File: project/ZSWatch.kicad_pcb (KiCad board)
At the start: 4 copper layers, 41 x 38 mm, 74 parts, among them IC1 nPM1300-QEXX, IC10 DRV2603RUNT, IC11 FAN5622SX, IC2 APDS-9306-065, IC3 BMI270, IC4 BMP581, IC5 BME688, IC6 LIS2MDLTR, IC7 ESDALC6V1W5, IC8 AT25SL128A, IC9 NTS0104GU12, M1 NORA-B106, Q1 BC817W, X1 BATTERY, X2 DOCK, X3 GC9A01A_CST816S, X4 M+, X5 M-

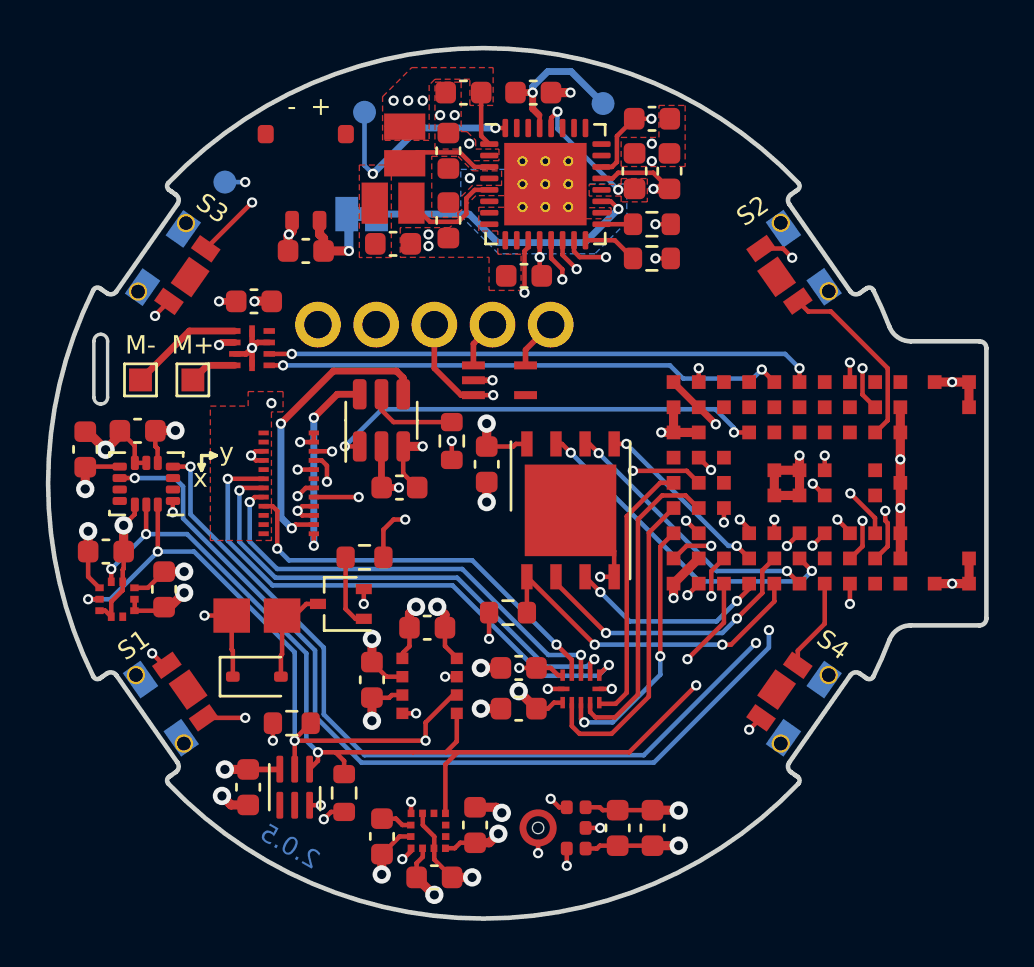
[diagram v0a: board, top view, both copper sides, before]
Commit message: - Add QR code library with link to the project - Change ISET resistor to 12k - Replace light sensor footprint with a version from our KiCad library - Rename the inner copper layers - Add KiBot file for production file generation - Import nPM1300 from test project - Remove pull down resistor from vibration driver IC enable - Split schematics into hierarical schematics - Add PCB variant for reduced sensor board - Add I2S microphone - Update all symbols and footprints - Move BTN_2 from P0.30 to P1.10 - Move BTN_3 from P1.12 to P0.31 - Move DRV_VIB_EN from P1.14 to P1.05 - Move BMI270_IN1 from P0.21 to P1.08 - Move BMI270_IN2 from P0.19 to P1.04 - Move DRV_VIB_PWM from P1.15 to P1.05 - Move DRV_VIB_EN from P1.05 to P1.15 - Move BTN_4 from P1.06 to P0.26 - Replace ESDALC6V1W5 with ESDALC6V1P5 - Add USB support (experimental) - Add marker for display cable orientation - Add markers for better IC placements - Replace the flash memory with WSON-8 variant to allow 64 MB devices - Remove old PCBWay documentation
Signed-off-by: Daniel Kampert <DanielKampert@kampis-elektroecke.de>
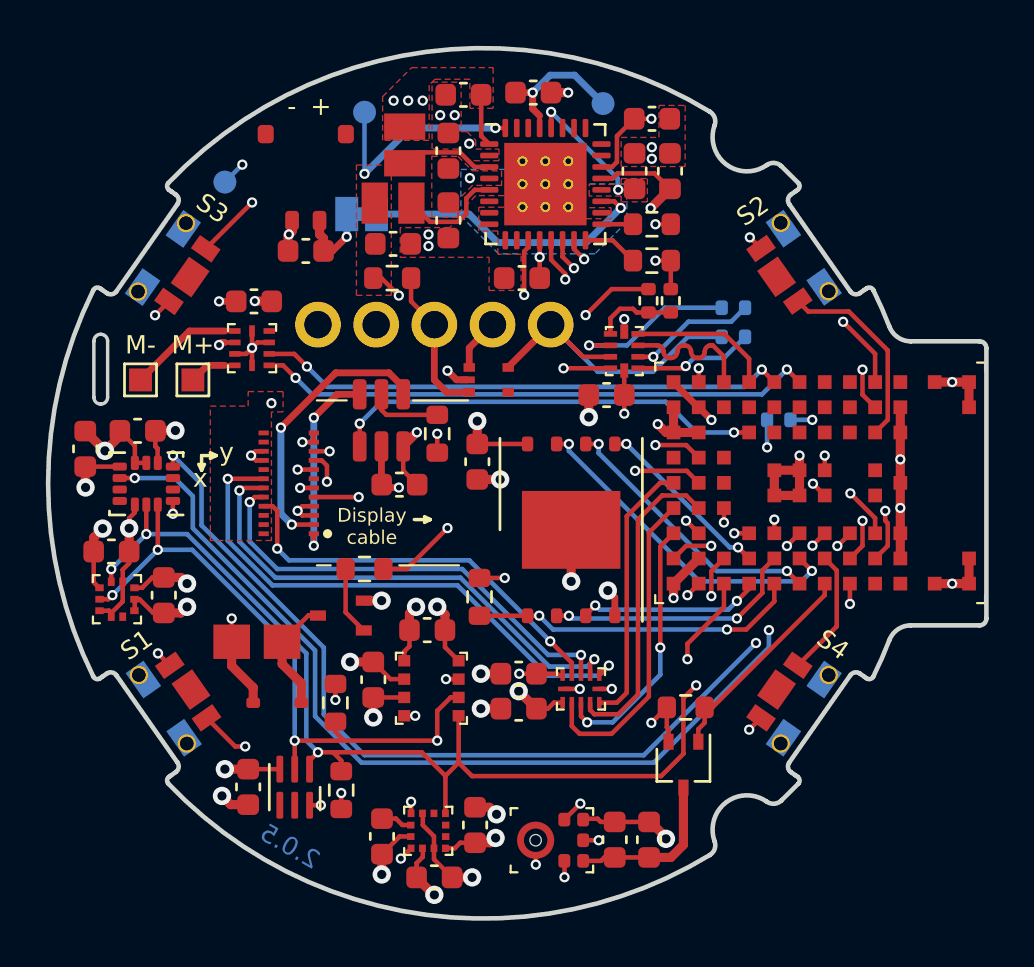
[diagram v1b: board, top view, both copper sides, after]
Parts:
- removed the C22 at (165.2, 127.8)
- added C24: 200p, Capacitor_SMD:C_0603_1608Metric, F.Cu at (166.6, 128.3)
- added C25: 100n, Capacitor_SMD:C_0603_1608Metric, F.Cu at (164.7, 108.9)
- added IC10: TS3USB221A, Package_QFN:UQFN-10_1.55x2.05mm_P0.5mm, F.Cu at (165.5, 106.9)
- added Q3: DMG1013UW-7, Package_TO_SOT_SMD:SOT-323_SC-70, F.Cu at (168.1, 125.0)
- added R10: 0R, Resistor_SMD:R_0402_1005Metric, F.Cu at (166.6, 104.7)
- added R11: 0R, Resistor_SMD:R_0402_1005Metric, B.Cu at (170.3, 105.1)
- added R12: 0R, Resistor_SMD:R_0402_1005Metric, B.Cu at (170.3, 106.3)
- added R13: 0R, Resistor_SMD:R_0402_1005Metric, F.Cu at (167.5, 104.7)
- added R14: 150k, Resistor_SMD:R_0603_1608Metric, F.Cu at (168.2, 122.5)
- added R8: 100k, Resistor_SMD:R_0603_1608Metric, F.Cu at (155.4, 103.8)
- added R9: 0R, Resistor_SMD:R_0402_1005Metric, B.Cu at (172.3, 109.9)
- C23: value 200p -> 1u
- IC7: footprint Package_SOT_SMD:SOT-325-5 -> Package_TO_SOT_SMD:SOT-665
- IC9: renamed from IC8; value AT25SL128A -> S25FS512SAGNFI010; footprint Package_DFN_QFN:DFN-8-1EP_6x5mm_P1.27mm_EP4x4mm -> Package_SON:WSON-8-1EP_8x6mm_P1.27mm_EP3.4x4.3mm
- moved R6 2.10 mm to (152.9, 122.3), turned to 90 degrees
- moved C23 1.73 mm to (165.1, 128.3)
- moved D1 1.45 mm to (150.4, 122.3)
- moved R4 1.42 mm to (159.2, 117.7), turned to -90 degrees
- moved BZ1 1.14 mm to (149.5, 119.6)
- moved IC9 0.85 mm to (163.2, 114.8)
- moved R3 0.71 mm to (157.4, 110.6)
- moved MK1 0.55 mm to (162.4, 128.3)
- moved R7 0.51 mm to (154.2, 116.5)
- moved Q1 0.51 mm to (153.1, 118.5)
- moved C22 0.43 mm to (159.1, 111.8)
- moved IC7 0.42 mm to (159.6, 108.2)
- moved C14 0.25 mm to (145.4, 117.6)
- moved C27 0.25 mm to (160.9, 121.0)
- moved C15 0.24 mm to (143.1, 115.7)
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- renumbered C18 to C17, C17 to C18, C20 to C19, C19 to C20, C27 to C21, C21 to C22, C24 to C26, C25 to C27, C26 to C28, IC9 to IC11, IC10 to IC12, IC6 to IC5, IC5 to IC6, IC11 to IC8, R7 to R3, R3 to R4, R4 to R5, R5 to R6, R6 to R7
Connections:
- net MIC_BCLK renamed /MCU/MIC_BCLK
- net MIC_DATA renamed /MCU/MIC_DATA
- net MIC_SEL renamed /MCU/MIC_SEL
- C20 pad 1: +1V8 -> GND
- C20 pad 2: GND -> +1V8
- C23 pad 2: +1V8 -> Net-(MK1-VDD)
- IC7 pad 1: SWDIO -> D-/SWDIO
- IC7 pad 3: RESETn -> SEL_SWD
- IC7 pad 5: SWDCLK -> D+/SWDCLK
- M1 pad C9: unconnected-(M1A-D+-PadC9) -> MCU_D_P
- M1 pad D9: unconnected-(M1A-D--PadD9) -> MCU_D_N
- M1 pad E9: DRV_VIB_EN -> DRV_VIB_PWM
- M1 pad F9: DRV_VIB_PWM -> DRV_VIB_EN
- M1 pad G1: BTN_4 -> /MCU/MIC_EN
- M1 pad G2: unconnected-(M1B-P0.26/AIN5-PadG2) -> BTN_4
- M1 pad H2: SWDIO -> MCU_SWDIO
- M1 pad H9: /MCU/PMIC-INT -> unconnected-(M1C-P1.11-PadH9)
- M1 pad J2: SWDCLK -> MCU_SWDCLK
- M1 pad J8: BTN_3 -> /MCU/PMIC-INT
- M1 pad J9: unconnected-(M1B-P0.31-PadJ9) -> BTN_3
- MK1 pad 5: +1V8 -> Net-(MK1-VDD)
- X2 pad 1: SWDCLK -> D+/SWDCLK
- X2 pad 2: SWDIO -> D-/SWDIO
- X2 pad 3: RESETn -> SEL_SWD
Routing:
- net SEL_SWD: track 0.00 -> 26.6 mm, vias 0 -> 2
- net SWDIO: track 26.1 -> 0.00 mm, vias 1 -> 0
- net SWDCLK: track 25.3 -> 0.00 mm, vias 1 -> 0
- net MCU_SWDIO: track 0.00 -> 21.9 mm, vias 0 -> 2
- net +3V0: track 37.4 -> 58.8 mm, vias 3 -> 6
- net MCU_SWDCLK: track 0.00 -> 21.1 mm, vias 0 -> 2
- net RESETn: track 26.3 -> 7.04 mm
- net D+/SWDCLK: track 0.00 -> 14.8 mm
- net D-/SWDIO: track 0.00 -> 14.6 mm, vias 0 -> 1
- net /MCU/MIC_EN: track 0.00 -> 9.39 mm
- net Net-(MK1-VDD): track 0.00 -> 7.17 mm
- net MCU_D_N: track 0.00 -> 6.32 mm
- net MCU_D_P: track 0.00 -> 6.24 mm
- net Net-(IC10-~{OE}): track 0.00 -> 3.55 mm
- net BTN_1: track 40.8 -> 38.7 mm
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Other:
- outline, holes or cut-outs redrawn
- board text added: "Display cable"

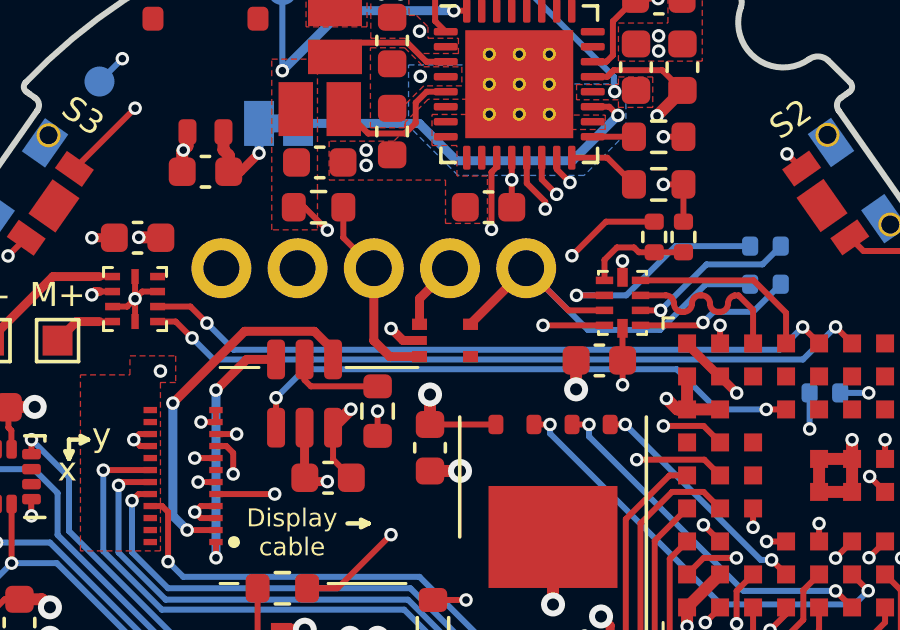
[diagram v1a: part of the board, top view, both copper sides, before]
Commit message: - Remove S1, S2 and S4 from Sensor variant - Remove microphone from Sensor variant - Update symbols - Add missing supply chain documentation - Update KiBot template to the newest version
Signed-off-by: Daniel Kampert <DanielKampert@kampis-elektroecke.de>
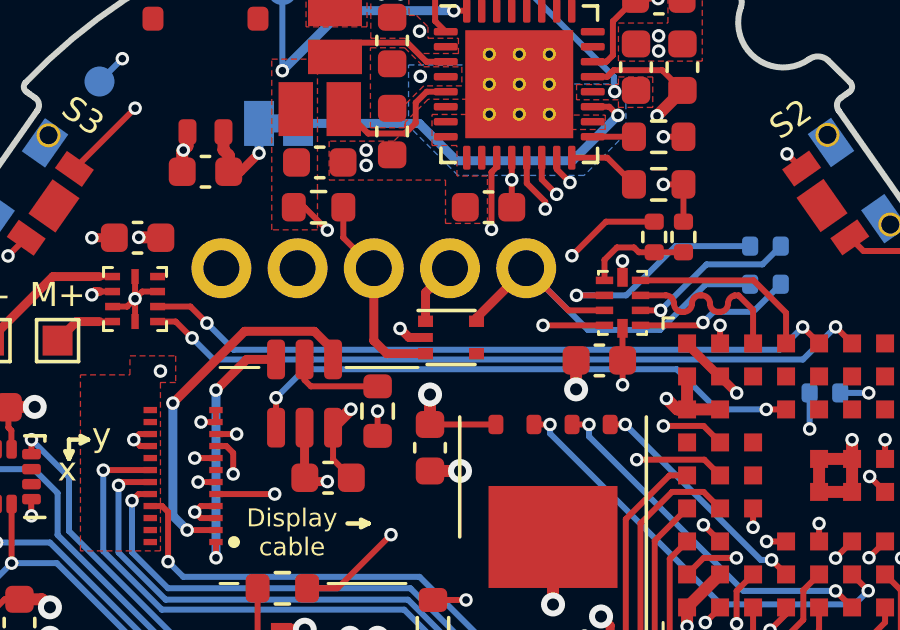
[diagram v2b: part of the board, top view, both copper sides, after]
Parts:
- moved IC7 0.22 mm to (159.8, 108.1)

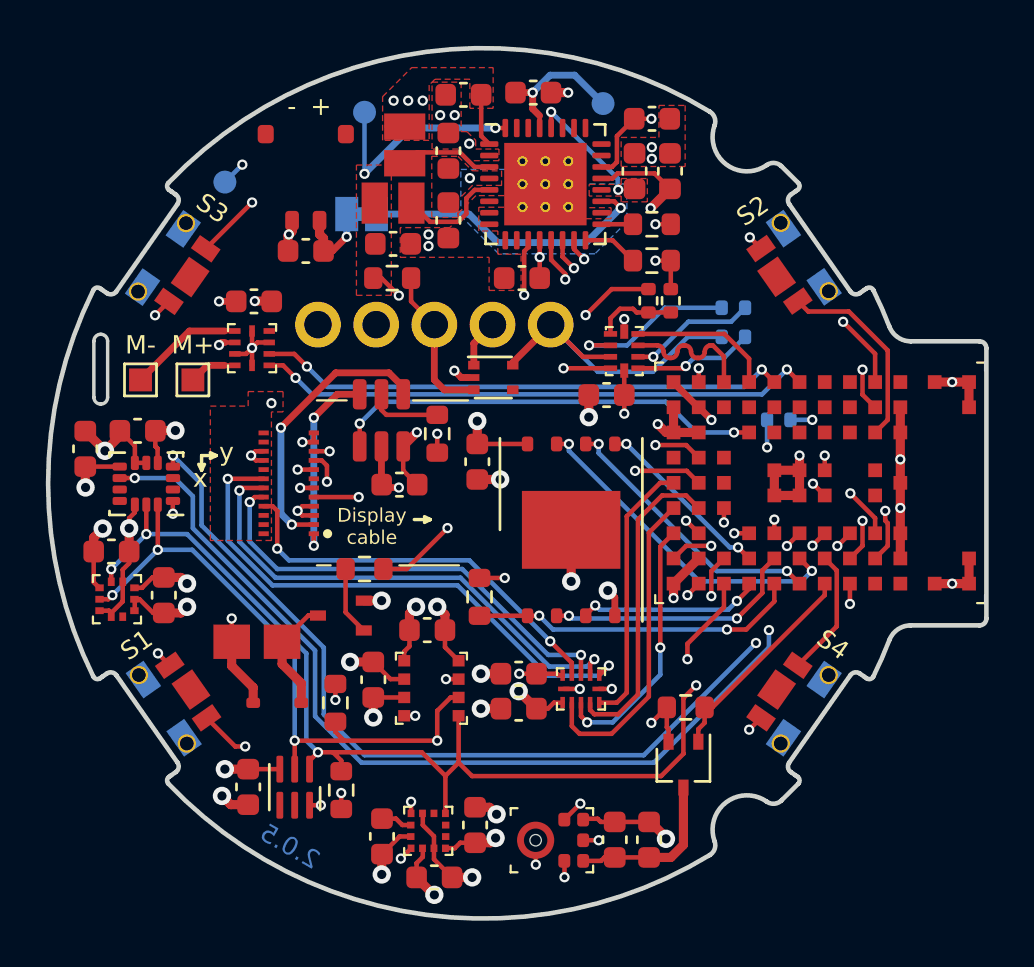
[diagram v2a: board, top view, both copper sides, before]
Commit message: - Set value for current measurement jumper
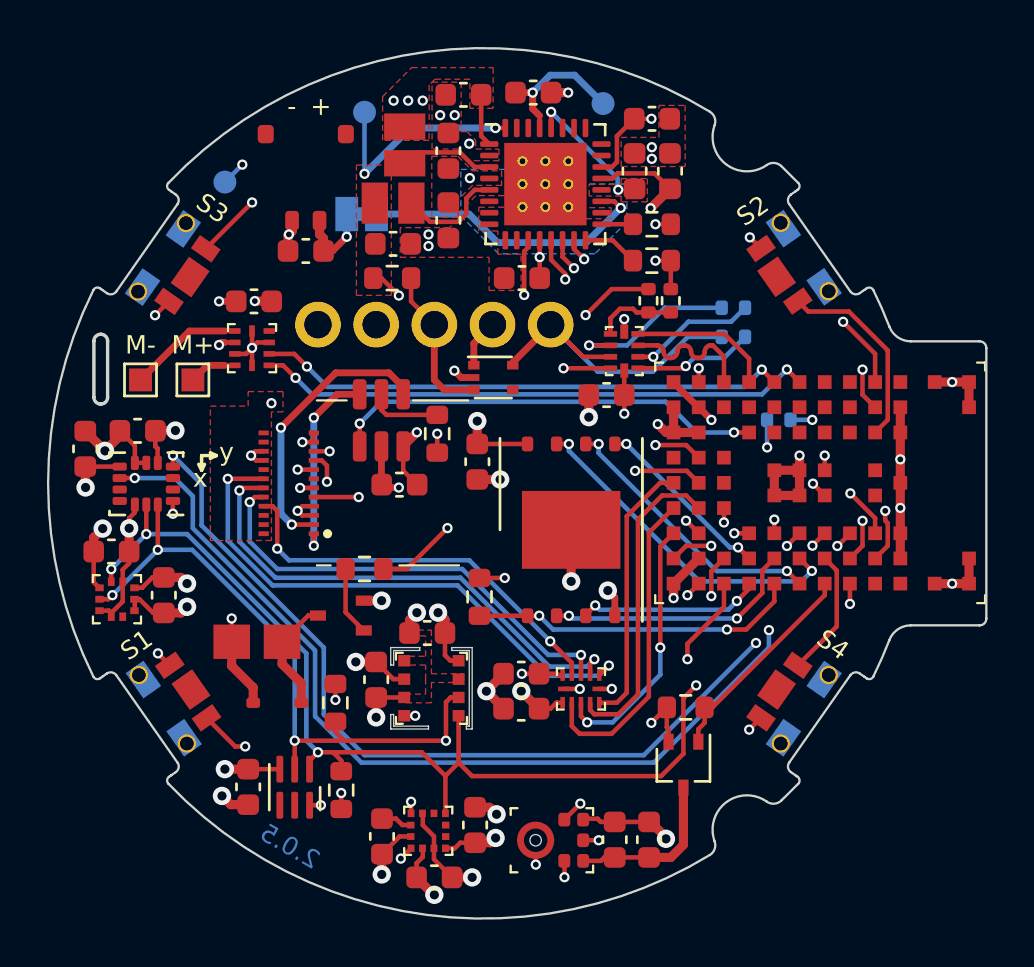
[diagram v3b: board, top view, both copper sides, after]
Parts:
- J1: value ~ -> CURRENT
- moved G*** 14.0 mm to (167.4, 118.2)
- moved G*** 4.95 mm to (159.1, 125.7)
- moved C18 0.13 mm to (154.7, 121.3)
- moved C20 0.13 mm to (156.9, 119.3)
- moved C26 0.11 mm to (161.0, 122.6)
- moved C27 0.11 mm to (161.0, 121.0)
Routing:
- net +1V8: track 47.5 -> 45.2 mm, vias 23 -> 22
- net GND: track 78.2 -> 78.3 mm, vias 52 -> 51
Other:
- outline, holes or cut-outs redrawn
- board text removed: "Display cable"

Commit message: - Remove old documentation - Update libraries - Rename signals - Update CHANGELOG
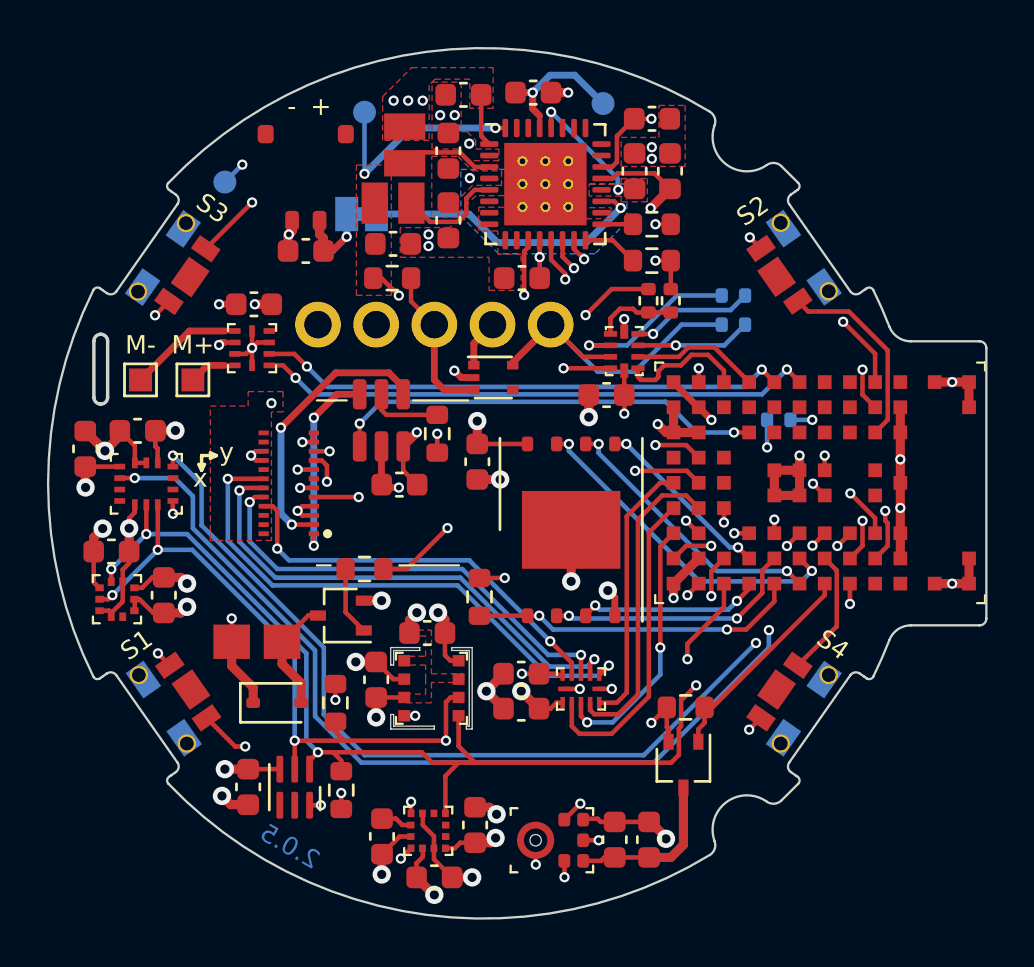
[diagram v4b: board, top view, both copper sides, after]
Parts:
- IC3: footprint Package_LGA:LGA-14_3x2.5mm_P0.5mm_LayoutBorder3x4y -> Package_LGA_Kampi:Bosch_LGA-14_3x2.5mm_P0.5mm_LayoutBorder3x4y
- moved R11 0.53 mm to (170.3, 104.5)
- moved R12 0.53 mm to (170.3, 105.8)
- moved C28 0.13 mm to (149.4, 104.9)
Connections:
- net /MCU/LIS2MDL_INT renamed /MCU/LIS2MDL-INT
- net /MCU/MIC_BCLK renamed /MCU/MIC-BCLK
- net /MCU/MIC_DATA renamed /MCU/MIC-DATA
- net /MCU/MIC_EN renamed /MCU/MIC-EN
- net /MCU/MIC_SEL renamed /MCU/MIC-SEL
- net BTN_1 renamed BTN-1
- net BTN_2 renamed BTN-2
- net BTN_3 renamed BTN-3
- net BTN_4 renamed BTN-4
- net DISPLAY_BLK renamed DISPLAY-BLK
- net DISPLAY_CLK renamed DISPLAY-CLK
- net DISPLAY_CS renamed DISPLAY-CS
- net DISPLAY_DATA renamed DISPLAY-DATA
- net DISPLAY_DC renamed DISPLAY-DC
- net DISPLAY_EN renamed DISPLAY-EN
- net DISPLAY_RST renamed DISPLAY-RST
- net DRV_VIB_EN renamed VIB-EN
- net DRV_VIB_PWM renamed VIB-PWM
- net QSPI_CLK renamed QSPI-CLK
- net QSPI_CS renamed QSPI-CS
- net QSPI_IO0 renamed QSPI-IO0
- net QSPI_IO1 renamed QSPI-IO1
- net QSPI_IO2 renamed QSPI-IO2
- net QSPI_IO3 renamed QSPI-IO3
- net SEL_SWD renamed SEL-SWD
- net TOUCH_INT renamed TOUCH-INT
- net TOUCH_RST renamed TOUCH-RST
- net TOUCH_SCL renamed TOUCH-SCL
- net TOUCH_SDA renamed TOUCH-SDA
- IC10 pad 1: MCU_SWDCLK -> MCU-D_P
- IC10 pad 2: MCU_SWDIO -> MCU-D_N
- IC10 pad 3: MCU_D_P -> MCU-SWDCLK
- IC10 pad 4: MCU_D_N -> MCU-SWDIO
- M1 pad C9: MCU_D_P -> MCU-D_P
- M1 pad D9: MCU_D_N -> MCU-D_N
- M1 pad H2: MCU_SWDIO -> MCU-SWDIO
- M1 pad J2: MCU_SWDCLK -> MCU-SWDCLK
- R11 pad 1: MCU_SWDIO -> MCU-SWDIO
- R12 pad 1: MCU_SWDCLK -> MCU-SWDCLK
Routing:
- net MCU-SWDIO: track 0.00 -> 22.8 mm, vias 0 -> 2
- net MCU-SWDCLK: track 0.00 -> 22.0 mm, vias 0 -> 2
- net MCU_SWDIO: track 21.9 -> 0.00 mm, vias 2 -> 0
- net MCU_SWDCLK: track 21.1 -> 0.00 mm, vias 2 -> 0
- net MCU_D_N: track 6.32 -> 0.00 mm
- net MCU_D_P: track 6.24 -> 0.00 mm
- net MCU-D_N: track 0.00 -> 5.65 mm
- net MCU-D_P: track 0.00 -> 5.57 mm
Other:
- outline, holes or cut-outs redrawn

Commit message: Update footprints
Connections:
- C28 pad 1: /MCU/VBAT -> /MCU/VBUS-MCU
- C3 pad 1: /MCU/VBAT -> /Power Management/VBAT
- IC12 pad 7: /MCU/VBAT -> /MCU/VBUS-MCU
- J1 pad 1: /MCU/VBAT -> /Power Management/VBAT
- X1 pad 1: /MCU/VBAT -> /Power Management/VBAT
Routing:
- net /MCU/VBUS-MCU: track 16.1 -> 43.7 mm, vias 2 -> 4
- net /MCU/VBAT: track 13.7 -> 0.00 mm, vias 3 -> 0
- net /Power Management/VBAT: track 0.00 -> 3.66 mm, vias 0 -> 1
